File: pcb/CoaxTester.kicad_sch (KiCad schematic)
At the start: 36 parts

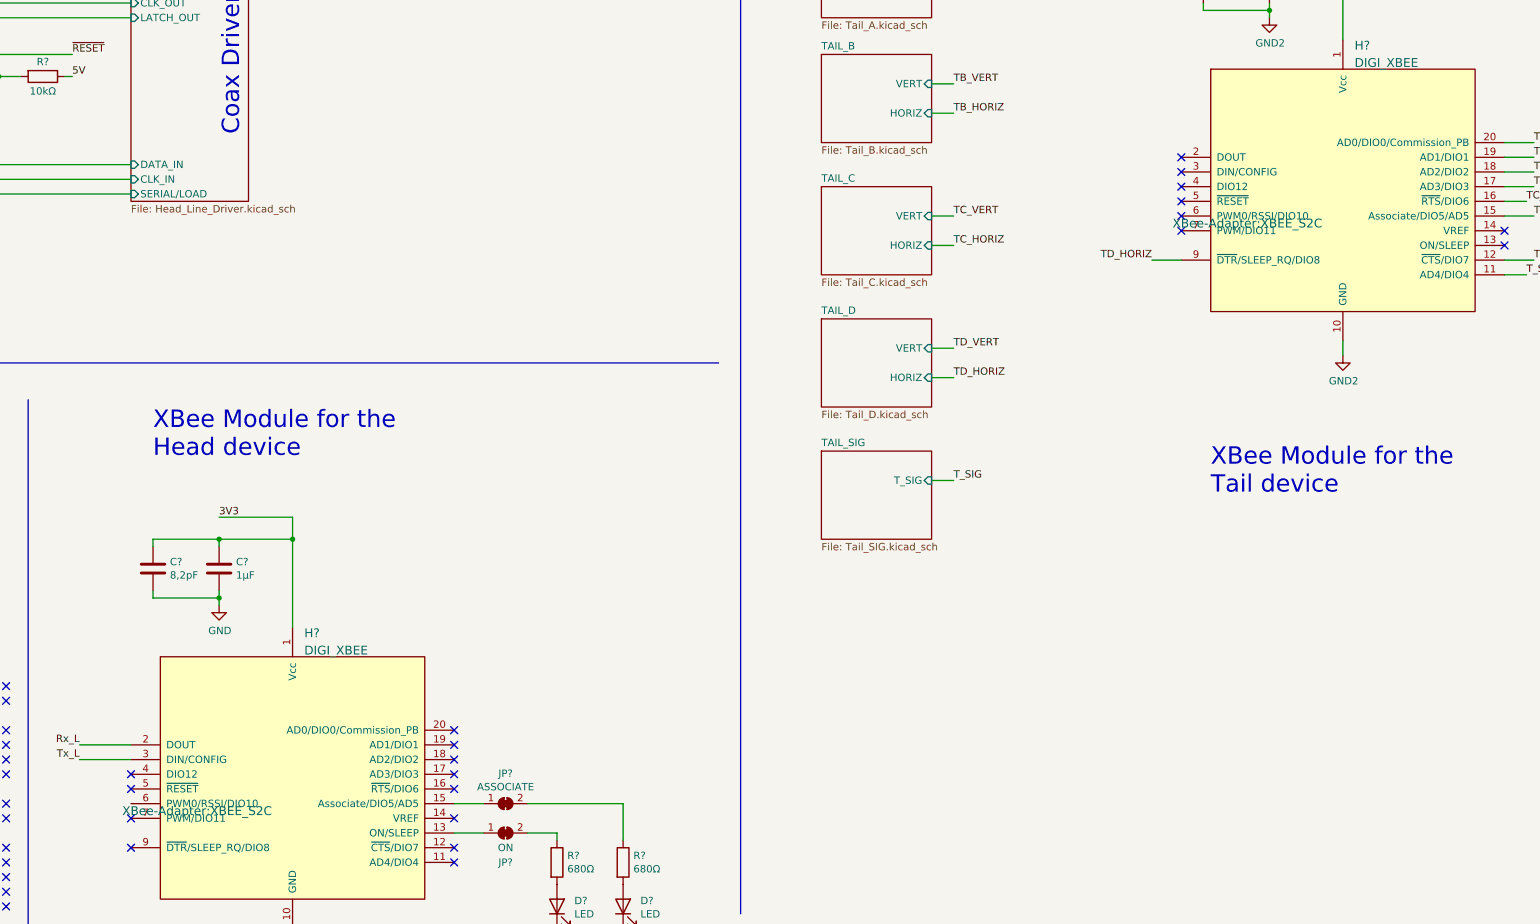
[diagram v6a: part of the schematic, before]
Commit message: Adds line protection
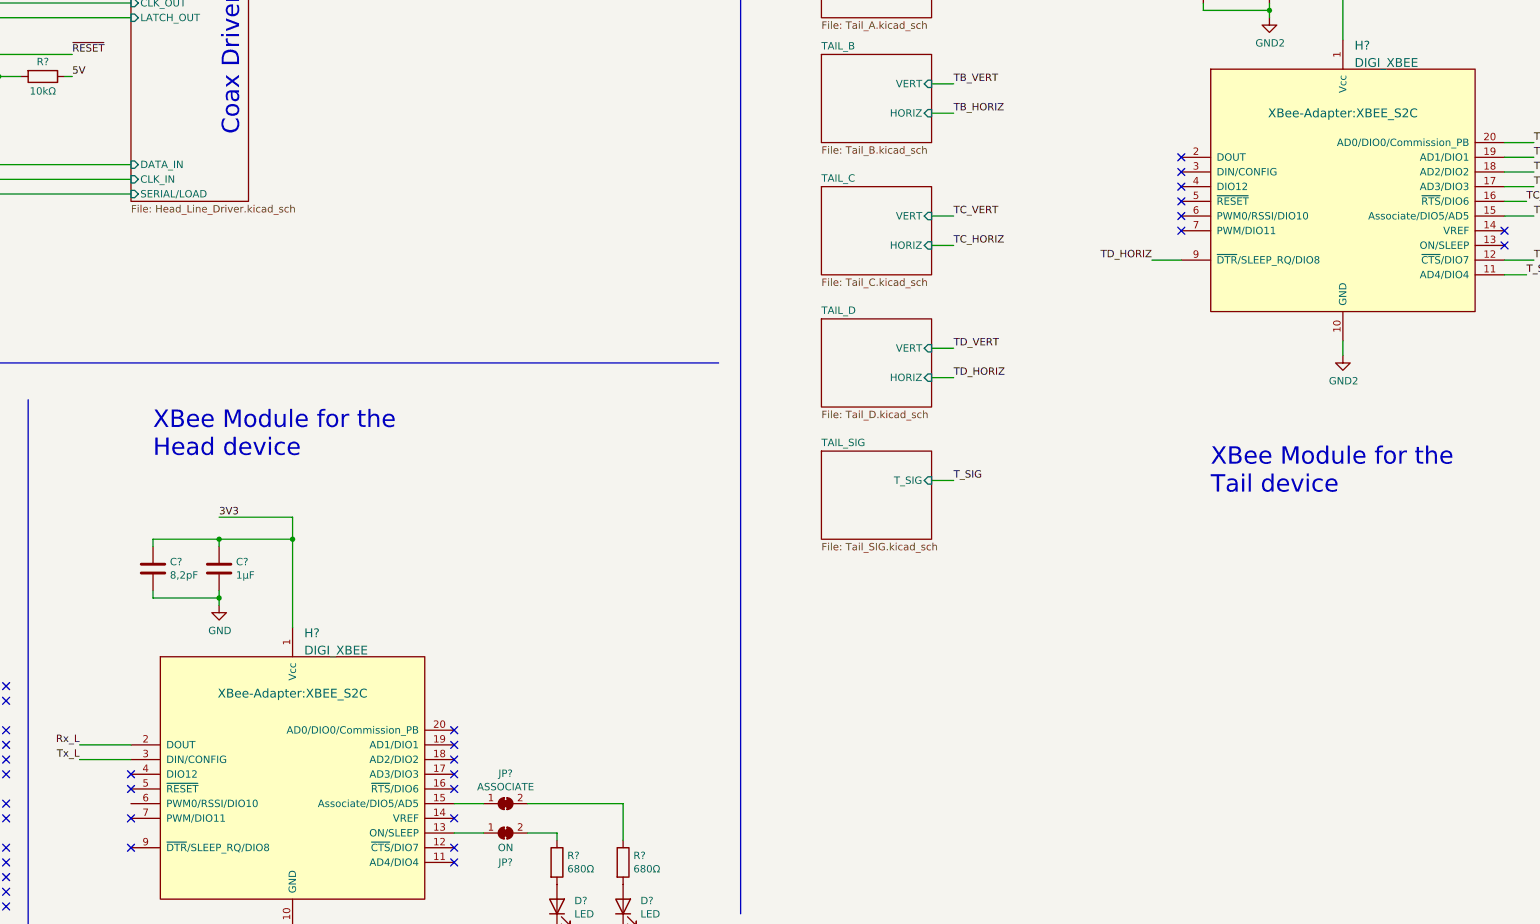
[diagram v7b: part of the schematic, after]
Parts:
- N? (x2): footprint (none) -> mech:Board Ref
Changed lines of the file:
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@@
       (effects (font (size 1.27 1.27)) (justify left))
     )
-    (property "Footprint" "" (id 2) (at 347.98 34.29 0)
+    (property "Footprint" "mech:Board Ref" (id 2) (at 347.98 34.29 0)
       (effects (font (size 1.27 1.27)) hide)
     )
@@
       (effects (font (size 1.27 1.27)) (justify left))
     )
-    (property "Footprint" "" (id 2) (at 186.69 35.56 0)
+    (property "Footprint" "mech:Board Ref" (id 2) (at 186.69 35.56 0)
       (effects (font (size 1.27 1.27)) hide)
     )
@@
   )
   (symbol (lib_id "XBee-Adapter:DIGI_XBEE") (at 170.18 228.6 0) (unit 1)
-    (in_bom yes) (on_board yes) (fields_autoplaced)
+    (in_bom yes) (on_board yes)
     (property "Reference" "H?" (id 0) (at 172.1994 202.9259 0)
       (effects (font (size 1.524 1.524)) (justify left))
@@
       (effects (font (size 1.524 1.524)) (justify left))
     )
-    (property "Footprint" "XBee-Adapter:XBEE_S2C" (id 2) (at 153.67 233.68 0)
+    (property "Footprint" "XBee-Adapter:XBEE_S2C" (id 2) (at 170.18 213.36 0)
       (effects (font (size 1.524 1.524)))
     )
@@
   )
   (symbol (lib_id "XBee-Adapter:DIGI_XBEE") (at 351.79 127 0) (unit 1)
-    (in_bom yes) (on_board yes) (fields_autoplaced)
+    (in_bom yes) (on_board yes)
     (property "Reference" "H?" (id 0) (at 353.8094 101.3259 0)
       (effects (font (size 1.524 1.524)) (justify left))
@@
       (effects (font (size 1.524 1.524)) (justify left))
     )
-    (property "Footprint" "XBee-Adapter:XBEE_S2C" (id 2) (at 335.28 132.08 0)
+    (property "Footprint" "XBee-Adapter:XBEE_S2C" (id 2) (at 351.79 113.03 0)
       (effects (font (size 1.524 1.524)))
     )
@@
       (reference "#PWR?") (unit 1) (value "GND") (footprint "")
     )
+    (path "/00000000-0000-0000-0000-000061c60b45/00000000-0000-0000-0000-000061c64a42/01926744-8292-4782-9b75-60d098a7a8f7"
+      (reference "#PWR?") (unit 1) (value "GND") (footprint "")
+    )
+    (path "/00000000-0000-0000-0000-000061c60b45/00000000-0000-0000-0000-000061c64a50/14374d6f-14e8-47c7-b086-00ea5385aabe"
+      (reference "#PWR?") (unit 1) (value "GND") (footprint "")
+    )
+    (path "/00000000-0000-0000-0000-000061b47bfa/20962b73-c378-4c45-9442-82007c0d2370"
+      (reference "#PWR?") (unit 1) (value "GND2") (footprint "")
+    )
+    (path "/00000000-0000-0000-0000-000061c60b45/00000000-0000-0000-0000-000061c64a57/2dd5a72a-4b35-4d33-98b9-3dc89f478048"
+      (reference "#PWR?") (unit 1) (value "GND") (footprint "")
+    )
+    (path "/00000000-0000-0000-0000-000061ae2aa5/3b175116-7f56-4e4b-b38e-e1190b602a7a"
+      (reference "#PWR?") (unit 1) (value "GND") (footprint "")
+    )
     (path "/00000000-0000-0000-0000-000061c60b45/488f05c2-7acd-4af4-aa90-1c1495a576e0"
       (reference "#PWR?") (unit 1) (value "GND") (footprint "")
     )
+    (path "/00000000-0000-0000-0000-000061c60b45/00000000-0000-0000-0000-000061c64a57/61fa4e2d-a7e6-48f6-8c99-82b219f7b2f5"
+      (reference "#PWR?") (unit 1) (value "GND") (footprint "")
+    )
     (path "/00000000-0000-0000-0000-000061c60b45/621f16cc-0225-480e-a2c6-d4d386ae8f5e"
       (reference "#PWR?") (unit 1) (value "GND") (footprint "")
@@
       (reference "#PWR?") (unit 1) (value "GND") (footprint "")
     )
+    (path "/00000000-0000-0000-0000-000061c60b45/00000000-0000-0000-0000-000061c64a49/9eea7bf9-cd7f-445e-b305-a2c026006a8b"
+      (reference "#PWR?") (unit 1) (value "GND") (footprint "")
+    )
     (path "/00000000-0000-0000-0000-000061c60b45/b1c2b919-2c89-412d-9eb8-2aa456907610"
       (reference "#PWR?") (unit 1) (value "GND") (footprint "")
@@
       (reference "#PWR?") (unit 1) (value "GND") (footprint "")
     )
+    (path "/00000000-0000-0000-0000-000061c60b45/00000000-0000-0000-0000-000061c64a5c/bbd905a6-42e0-4b89-b25f-54bd37109430"
+      (reference "#PWR?") (unit 1) (value "GND") (footprint "")
+    )
     (path "/c224753b-c3cc-412e-b299-999953063464"
+      (reference "#PWR?") (unit 1) (value "GND") (footprint "")
+    )
+    (path "/00000000-0000-0000-0000-000061c60b45/00000000-0000-0000-0000-000061c64a50/cd10839d-fb7d-4c76-8120-aa8657e54295"
+      (reference "#PWR?") (unit 1) (value "GND") (footprint "")
+    )
+    (path "/00000000-0000-0000-0000-000061c60b45/00000000-0000-0000-0000-000061c64a42/d2a641d1-bd0c-4130-8327-3ea0fadc171c"
+      (reference "#PWR?") (unit 1) (value "GND") (footprint "")
+    )
+    (path "/00000000-0000-0000-0000-000061c60b45/00000000-0000-0000-0000-000061c64a49/dfcf2473-c682-4387-9731-ab3c9bdebf42"
       (reference "#PWR?") (unit 1) (value "GND") (footprint "")
     )
@@
       (reference "D?") (unit 1) (value "LED") (footprint "LED_SMD:LED_0805_2012Metric")
     )
+    (path "/00000000-0000-0000-0000-000061c60b45/00000000-0000-0000-0000-000061c64a50/46e99d99-c915-4f17-9d64-939dc4cb5a32"
+      (reference "D?") (unit 1) (value "SMDB03C") (footprint "Package_SO:SO-8_3.9x4.9mm_P1.27mm")
+    )
+    (path "/00000000-0000-0000-0000-000061c60b45/00000000-0000-0000-0000-000061c64a5c/98cadc57-1796-4441-a7e5-48beb9a53e19"
+      (reference "D?") (unit 1) (value "SMDB03C") (footprint "Package_SO:SO-8_3.9x4.9mm_P1.27mm")
+    )
     (path "/9e885b90-070c-44ee-a862-66cb7a82bcb6"
       (reference "D?") (unit 1) (value "LED") (footprint "LED_SMD:LED_0805_2012Metric")
     )
+    (path "/00000000-0000-0000-0000-000061c60b45/00000000-0000-0000-0000-000061c64a42/af148195-40ab-4e59-b0e8-8c7c263a4678"
+      (reference "D?") (unit 1) (value "SMDB03C") (footprint "Package_SO:SO-8_3.9x4.9mm_P1.27mm")
+    )
+    (path "/00000000-0000-0000-0000-000061c60b45/00000000-0000-0000-0000-000061c64a50/4bfd4c0b-e3f5-4b49-8aa9-33d4f4aa436c"
+      (reference "D?") (unit 2) (value "SMDB03C") (footprint "Package_SO:SO-8_3.9x4.9mm_P1.27mm")
+    )
+    (path "/00000000-0000-0000-0000-000061c60b45/00000000-0000-0000-0000-000061c64a42/dc325f15-a50a-4a7e-bad8-256b146c1e59"
+      (reference "D?") (unit 2) (value "SMDB03C") (footprint "Package_SO:SO-8_3.9x4.9mm_P1.27mm")
+    )
+    (path "/00000000-0000-0000-0000-000061c60b45/00000000-0000-0000-0000-000061c64a57/8d98a2e5-b0e2-4ec3-9a4a-e24f690c7510"
+      (reference "D?") (unit 3) (value "SMDB03C") (footprint "Package_SO:SO-8_3.9x4.9mm_P1.27mm")
+    )
+    (path "/00000000-0000-0000-0000-000061c60b45/00000000-0000-0000-0000-000061c64a49/92b39ff3-8845-461e-818d-9879615c6186"
+      (reference "D?") (unit 3) (value "SMDB03C") (footprint "Package_SO:SO-8_3.9x4.9mm_P1.27mm")
+    )
+    (path "/00000000-0000-0000-0000-000061c60b45/00000000-0000-0000-0000-000061c64a57/3d4e934a-9e7f-497e-a8db-b9e0e23c8695"
+      (reference "D?") (unit 4) (value "SMDB03C") (footprint "Package_SO:SO-8_3.9x4.9mm_P1.27mm")
+    )
+    (path "/00000000-0000-0000-0000-000061c60b45/00000000-0000-0000-0000-000061c64a49/53e5c5f5-c090-45d4-99c6-821d1803e2e4"
+      (reference "D?") (unit 4) (value "SMDB03C") (footprint "Package_SO:SO-8_3.9x4.9mm_P1.27mm")
+    )
     (path "/161d40b4-c790-4f3e-b1de-afef88fe8749"
       (reference "H?") (unit 1) (value "MountingHole") (footprint "MountingHole:MountingHole_3.2mm_M3")
@@
     )
     (path "/40b30d9a-4fb0-4992-8f57-b9024316f667"
-      (reference "N?") (unit 1) (value "Tail Enclosure") (footprint "")
+      (reference "N?") (unit 1) (value "Tail Enclosure") (footprint "mech:Board Ref")
     )
     (path "/5a58d39a-2ec3-4ef0-abec-6ec66d1cf4f2"
-      (reference "N?") (unit 1) (value "Head Enclosure") (footprint "")
+      (reference "N?") (unit 1) (value "Head Enclosure") (footprint "mech:Board Ref")
     )
     (path "/00000000-0000-0000-0000-000061bf30ef"
@@
     )
     (path "/00000000-0000-0000-0000-000061c60b45/0d010bf0-c540-4dc3-9fc7-b78c5a5efaa3"
-      (reference "U?") (unit 1) (value "74AHC595") (footprint "")
+      (reference "U?") (unit 1) (value "74AHC595") (footprint "Package_SO:SO-16_3.9x9.9mm_P1.27mm")
     )
     (path "/00000000-0000-0000-0000-000061c60b45/1919ed21-05d7-49ed-9bbf-ad716adf4104"
-      (reference "U?") (unit 1) (value "74HC165") (footprint "")
+      (reference "U?") (unit 1) (value "74HC165") (footprint "Package_SO:SO-16_3.9x9.9mm_P1.27mm")
     )
     (path "/00000000-0000-0000-0000-000061c60b45/36131634-c3ac-4133-a779-a13125d5274d"
-      (reference "U?") (unit 1) (value "74HC165") (footprint "")
+      (reference "U?") (unit 1) (value "74HC165") (footprint "Package_SO:SO-16_3.9x9.9mm_P1.27mm")
     )
     (path "/00000000-0000-0000-0000-000061c60b45/5e5b639c-5d7d-4123-8e20-13b394e8ce1b"
-      (reference "U?") (unit 1) (value "74AHC595") (footprint "")
+      (reference "U?") (unit 1) (value "74AHC595") (footprint "Package_SO:SO-16_3.9x9.9mm_P1.27mm")
     )
     (path "/00000000-0000-0000-0000-000061b6893f/d08e8c20-b451-4a9c-b796-97a4679a5100"

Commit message: Adds further features to the design
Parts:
- removed Q? (x2): IRLML2502, Micro3, symbol Tfac-Symbols:IRLML2502
- removed R? (x4): 10kΩ, Resistor_SMD:R_0805_2012Metric, symbol Device:R
- added C? (x10): 1μF, Capacitor_SMD:C_0805_2012Metric, symbol Device:C
- added D?: HEARTBEAT, LED_SMD:LED_0805_2012Metric, symbol Device:LED
- added Q?: IRLML2502, tfac-footprints:Micro3, symbol Tfac-Symbols:IRLML2502
- added R? (x3): 47Ω, Resistor_SMD:R_0805_2012Metric, symbol Device:R
- added R?: 680Ω, Resistor_SMD:R_0805_2012Metric, symbol Device:R
- added SW?: BACK_LT, Connector_PinHeader_2.54mm:PinHeader_1x02_P2.54mm_Vertical, symbol Switch:SW_Push
- added SW?: START, Connector_PinHeader_2.54mm:PinHeader_1x02_P2.54mm_Vertical, symbol Switch:SW_Push
- added U?: NLSX3012DR2G, Package_SO:SOIC-8-N7_3.9x4.9mm_P1.27mm, symbol CoaxTester:NLSX3012DR2G
- added U?: 74LS04, LED_Chain:SOIC-14, symbol 74xx:74LS04
- added U?: EA_DOGM128X-6, CoaxTester:EA_DOGM128-6, symbol Display_Graphic:EA_DOGM128X-6
- D?: value LED -> XB_ON
- D?: value LED -> XB_ASSOC
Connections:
- net 3V3: now also Q?.3 (D), U?.1 (V_{L}), U?.34 (VDD2), U?.35 (VDD)
- net 5V: now also U?.8 (V_{CC})
- net GND: now also U?.21 (GND), U?.3 (GND), U?.5 (GND), C?.2, C?.2, C?.2, C?.2, C?.2, C?.2, D?.1 (K), R?.2, R?.2, R?.2, SW?.2, SW?.2, U?.26 (VSS), U?.33 (VSS), U?.4 (GND)
- net GND2: no longer U?.21 (GND), U?.3 (GND), U?.5 (GND)
- net MOSI: now also U?.36 (SI)
- net Rx_H: now also U?.2 (I/O_V_{L}1)
- net Rx_L: now also U?.7 (I/O_V_{cc}1)
- net SCK: now also U?.37 (SCL)
- net Tx_H: now also U?.3 (I/O_V_{L}2)
- net Tx_L: now also U?.6 (I/O_V_{cc}2)
- net ~{XB_SLEEP}: now reaches U?.1 (PD3)
- net ~{XB_SLEEP}: now also H?.9 (~{DTR}/SLEEP_RQ/DIO8), U?.1
- net at U?.11 (PD7): now also R?.1
- net ~{DISP_REST}: now reaches U?.13 (PB1)
- net ~{DISP_REST}: now also U?.39 (~{RST})
- net ~{DISP_CS}: now reaches U?.14 (PB2)
- net ~{DISP_CS}: now also U?.40 (~{CS1B})
- net DISP_BKLT: now reaches U?.26 (PC3)
- net DISP_BKLT: now also Q?.1 (G)
- net ~{START}: now reaches U?.27 (PC4)
- net ~{START}: now also SW?.1
- net ~{BKLT}: now reaches U?.28 (PC5)
- net ~{BKLT}: now also SW?.1
- net ~{XB_RESET}: now reaches U?.32 (PD2)
- net ~{XB_RESET}: now also H?.5 (~{RESET})
- new net: C?.1, C?.2
- new net: C?.2, U?.31 (CAP3P)
- new net: C?.1, U?.29 (CAP1P)
- new net: C?.1, C?.2, U?.30 (CAP1N)
- new net: U?.2, U?.5 (EN)
- new net: R?.1, U?.20 (C3-)
- new net: R?.1, U?.19 (C2-)
- new net: C?.1, U?.24 (V3)
- new net: C?.1, U?.23 (V2)
- new net: R?.1, U?.18 (C1-)
- new net: C?.1, U?.21 (V0)
- new net: D?.2 (A), R?.2
- new net: C?.1, U?.25 (V4)
- new net: C?.1, U?.22 (V1)
- new net: Q?.2 (S), U?.1 (A1+), U?.2 (A2+), U?.3 (A3+)
- new net: C?.1, U?.32 (VOUT)
- new net: C?.1, U?.27 (CAP2N)
- new net: C?.2, U?.28 (CAP2P)
- new net A0: U?.38 (A0)
- no-connect marks 49 -> 27
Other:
- note added: "Check this connection and usage."
- note added: "Food for Thought. * Power ON indicator LED. * Heartbead diag. LED (dual colour) * Verify the mechanical construction of the switches."
- note added: "See about a dual-colour LED instead of two seperate LEDs."
- note removed: "Level Shifter https://tinyurl.com/y2q4nzwh"
- moved on the sheet: C?, R?, U?
